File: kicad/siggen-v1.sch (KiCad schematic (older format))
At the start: 0 parts

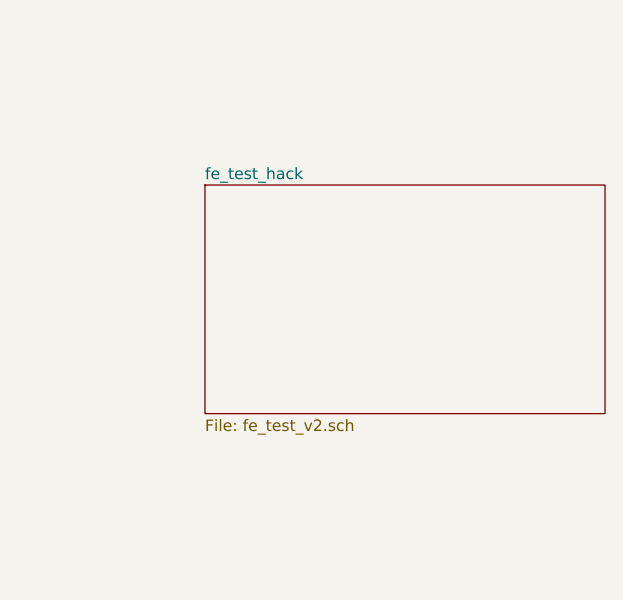
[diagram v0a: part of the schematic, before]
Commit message: removed frontent/amp test circuit
This circuit had shared the PCB for cost reasons.
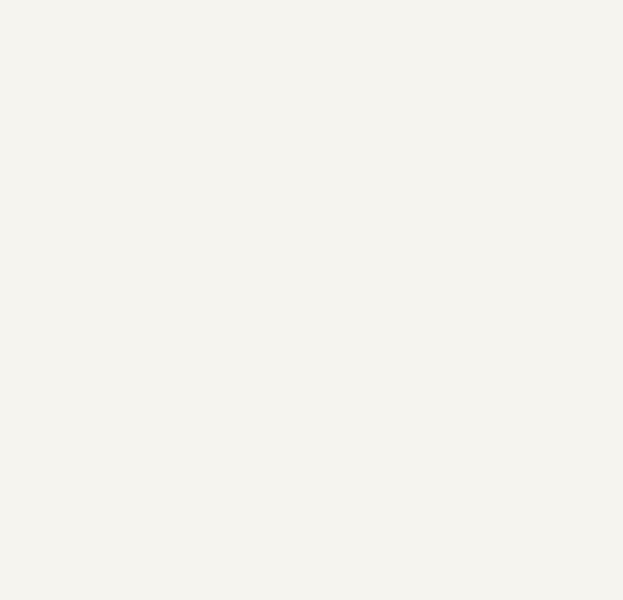
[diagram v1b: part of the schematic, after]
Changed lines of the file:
@@
 $Descr A4 11693 8268
 encoding utf-8
-Sheet 1 5
+Sheet 1 4
 Title ""
 Date ""
@@
 F1 "power.sch" 50
 $EndSheet
-$Sheet
-S 7050 3650 1750 1000
-U 6244652F
-F0 "fe_test_hack" 50
-F1 "fe_test_v2.sch" 50
-$EndSheet
 $EndSCHEMATC
